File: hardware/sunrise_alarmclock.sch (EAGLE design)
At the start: 26 parts, among them IC1 ATMEGA328P, IC2 WTV020, IC3 TinyRTC, IC4 HC-05, IC5 LD117AS33TR

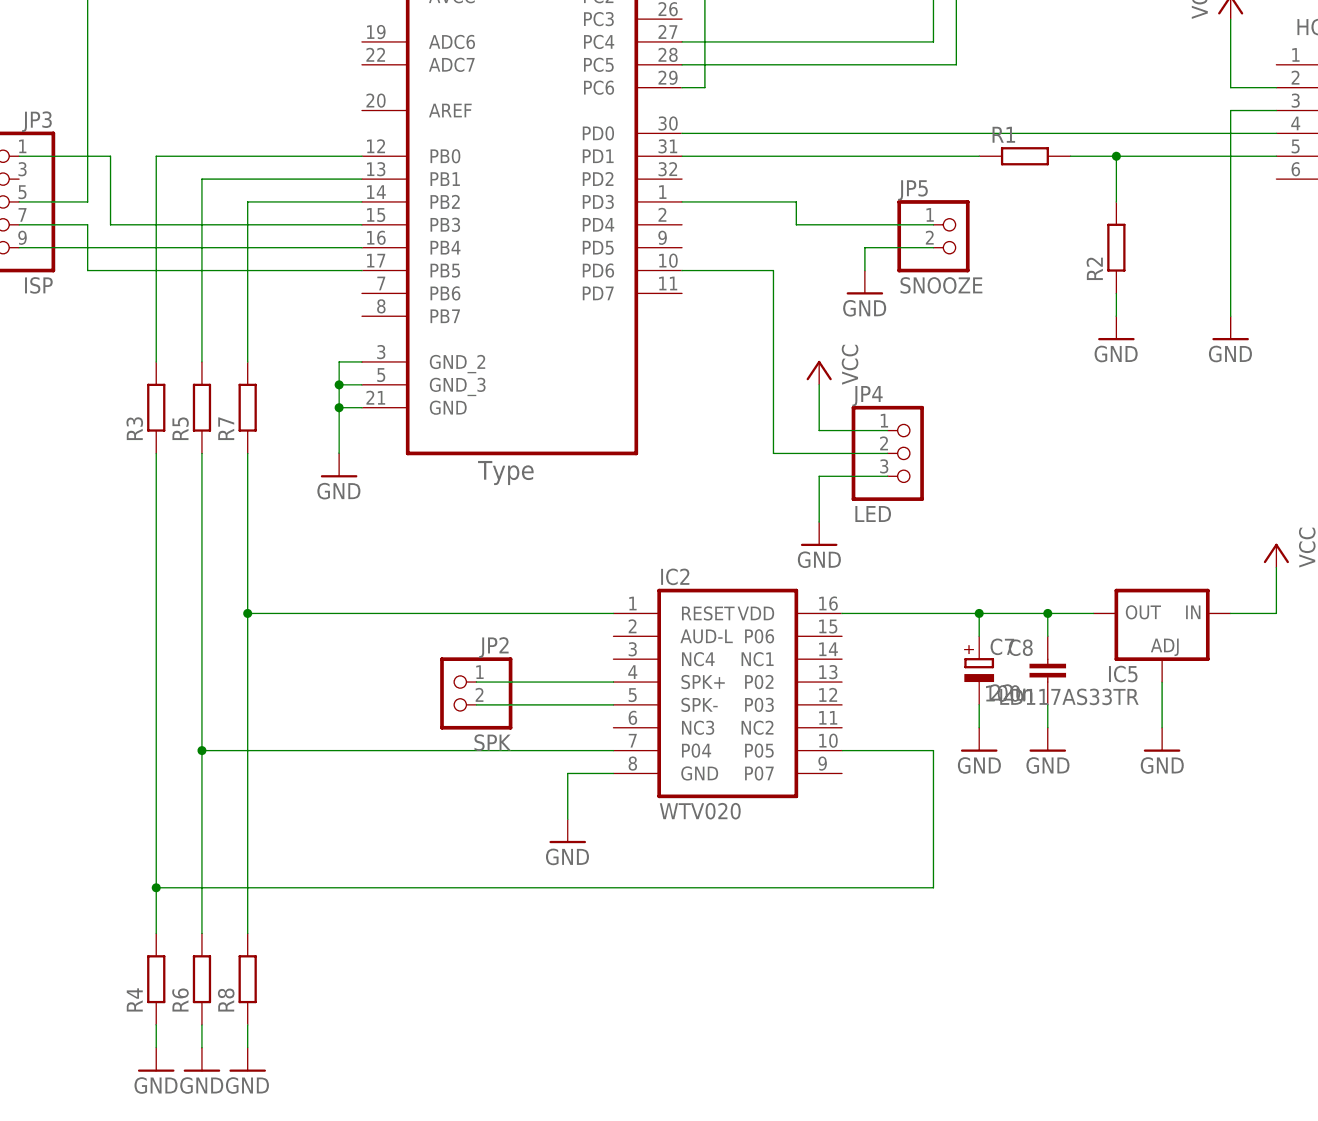
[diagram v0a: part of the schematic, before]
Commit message: hardware: added components values
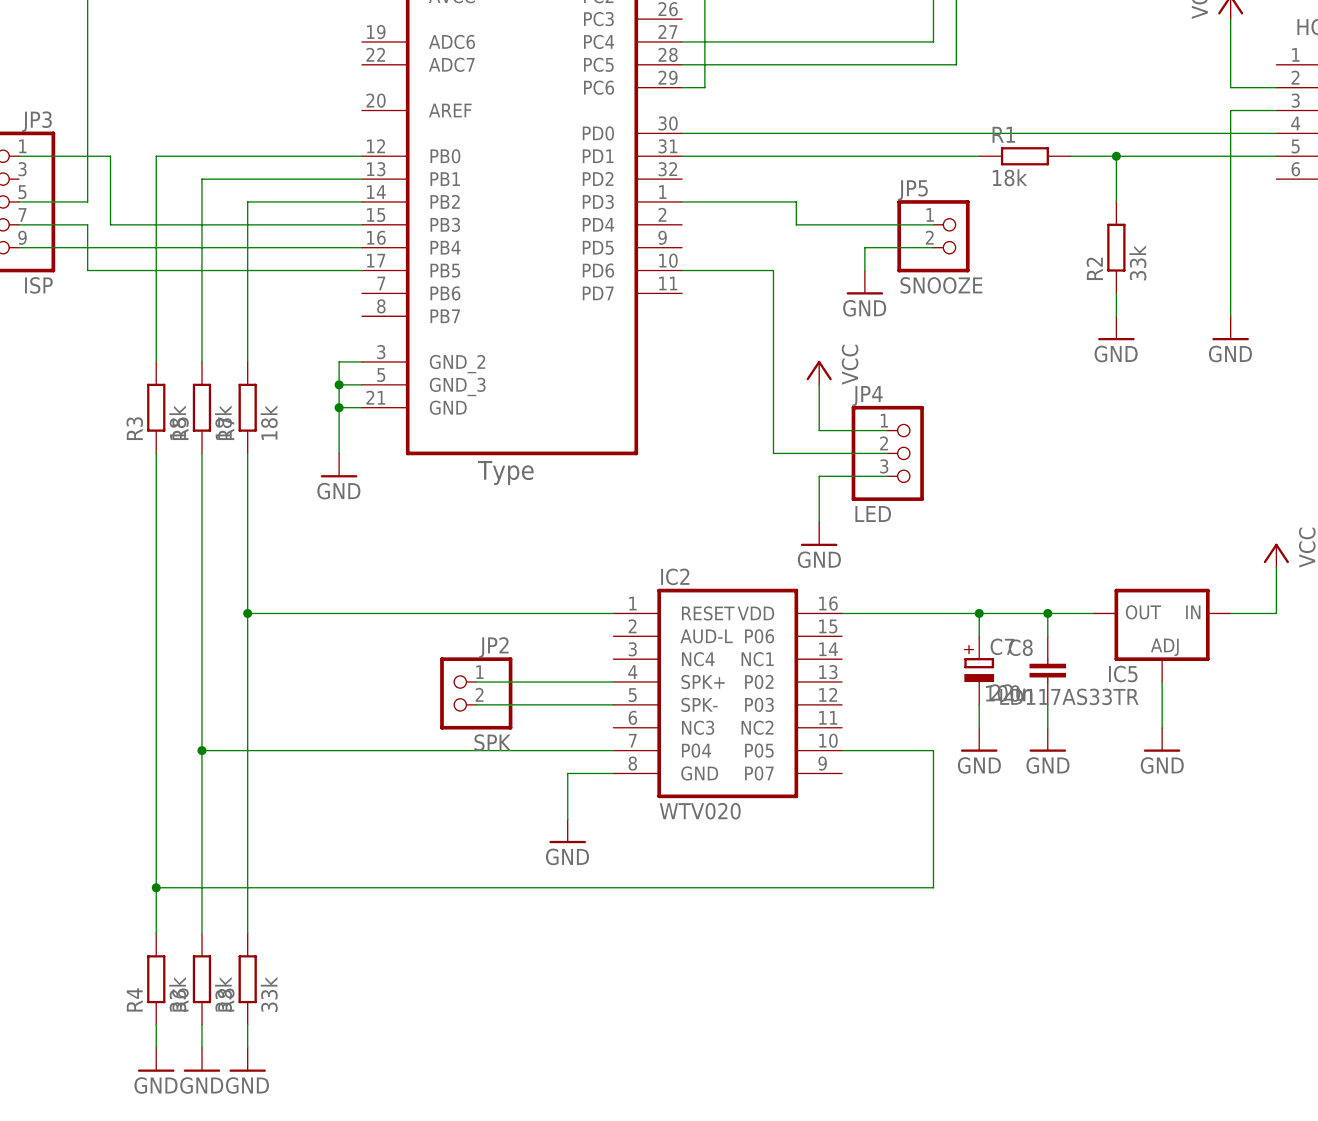
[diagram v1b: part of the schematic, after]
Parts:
- R1, R3, R5, R7: value (none) -> 18k
- R2, R4, R6, R8: value (none) -> 33k
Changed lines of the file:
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@@
 <part name="P+3" library="supply1" deviceset="VCC" device=""/>
 <part name="IC3" library="TinyRTC_module" deviceset="HC-05" device="" value="TinyRTC"/>
-<part name="R1" library="rcl" deviceset="R-EU_" device="M1206"/>
-<part name="R2" library="rcl" deviceset="R-EU_" device="M1206"/>
+<part name="R1" library="rcl" deviceset="R-EU_" device="M1206" value="18k"/>
+<part name="R2" library="rcl" deviceset="R-EU_" device="M1206" value="33k"/>
 <part name="C2" library="rcl" deviceset="C-EU" device="C1206K" value="100n"/>
 <part name="C3" library="rcl" deviceset="C-EU" device="C1206K" value="100n"/>
@@
 <part name="C8" library="rcl" deviceset="C-EU" device="C1206K" value="100n"/>
 <part name="GND7" library="supply1" deviceset="GND" device=""/>
-<part name="R3" library="rcl" deviceset="R-EU_" device="M1206"/>
-<part name="R5" library="rcl" deviceset="R-EU_" device="M1206"/>
-<part name="R7" library="rcl" deviceset="R-EU_" device="M1206"/>
-<part name="R4" library="rcl" deviceset="R-EU_" device="M1206"/>
-<part name="R6" library="rcl" deviceset="R-EU_" device="M1206"/>
-<part name="R8" library="rcl" deviceset="R-EU_" device="M1206"/>
+<part name="R3" library="rcl" deviceset="R-EU_" device="M1206" value="18k"/>
+<part name="R5" library="rcl" deviceset="R-EU_" device="M1206" value="18k"/>
+<part name="R7" library="rcl" deviceset="R-EU_" device="M1206" value="18k"/>
+<part name="R4" library="rcl" deviceset="R-EU_" device="M1206" value="33k"/>
+<part name="R6" library="rcl" deviceset="R-EU_" device="M1206" value="33k"/>
+<part name="R8" library="rcl" deviceset="R-EU_" device="M1206" value="33k"/>
 <part name="GND10" library="supply1" deviceset="GND" device=""/>
 <part name="GND11" library="supply1" deviceset="GND" device=""/>

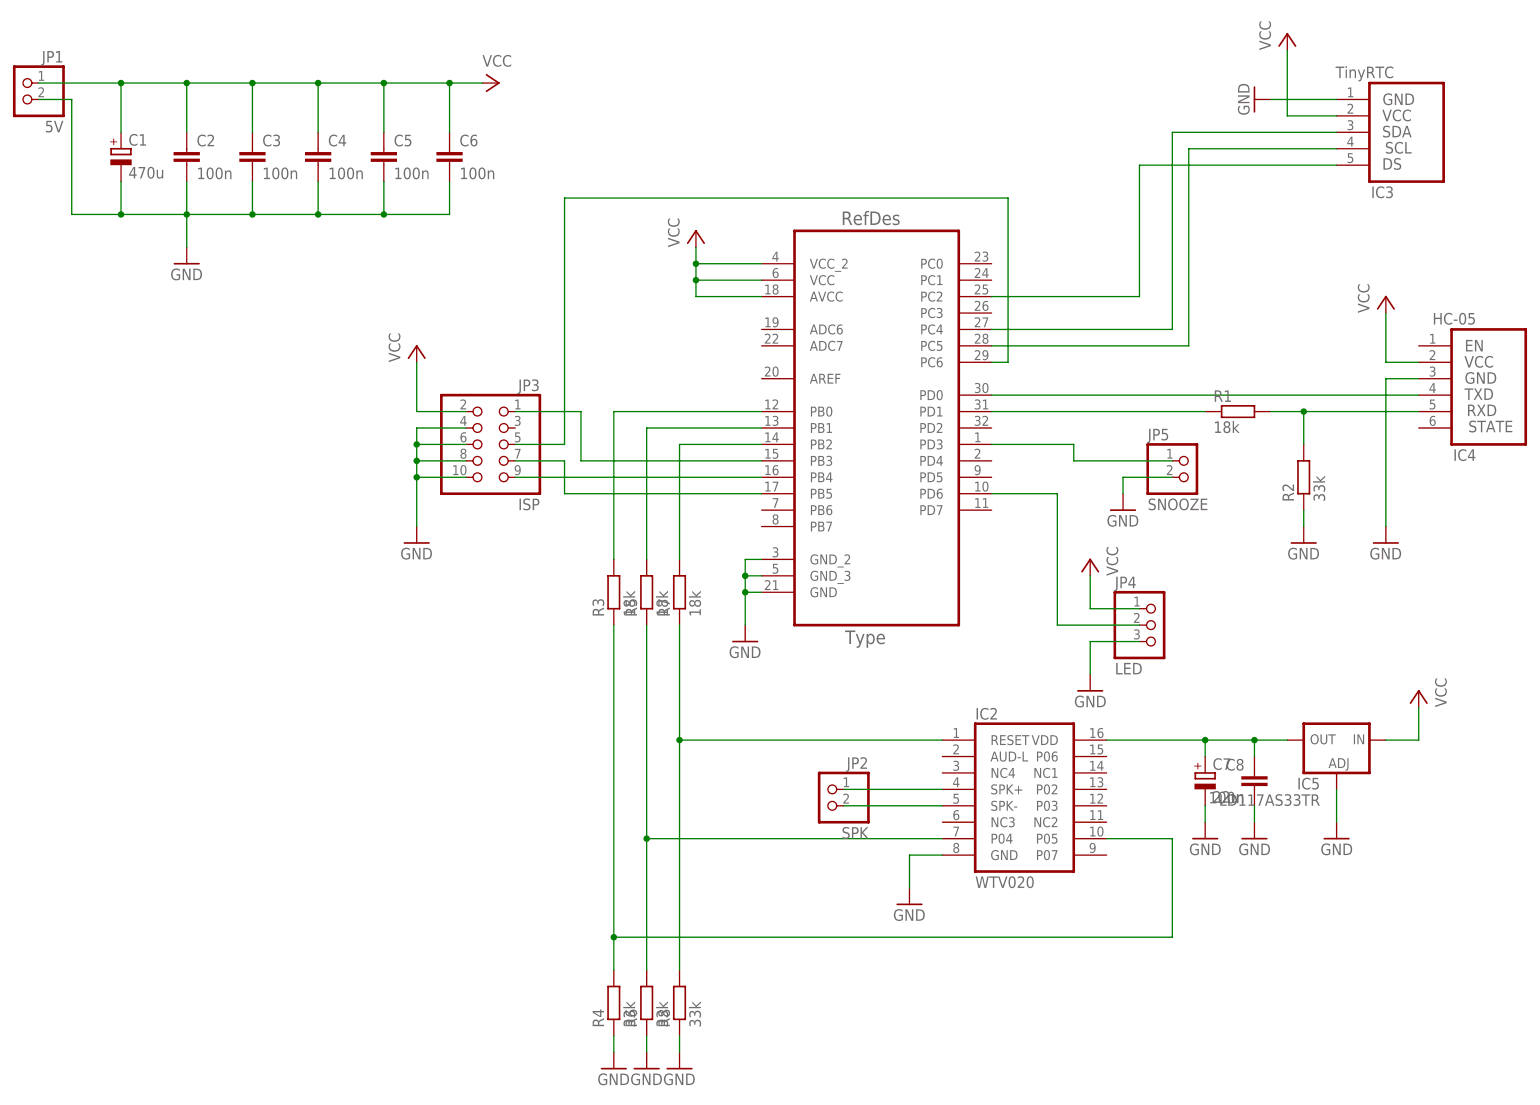
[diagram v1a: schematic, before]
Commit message: hardware: fixed values of resistor towards the voice module. added note about connection of photo resistor to pin PC1
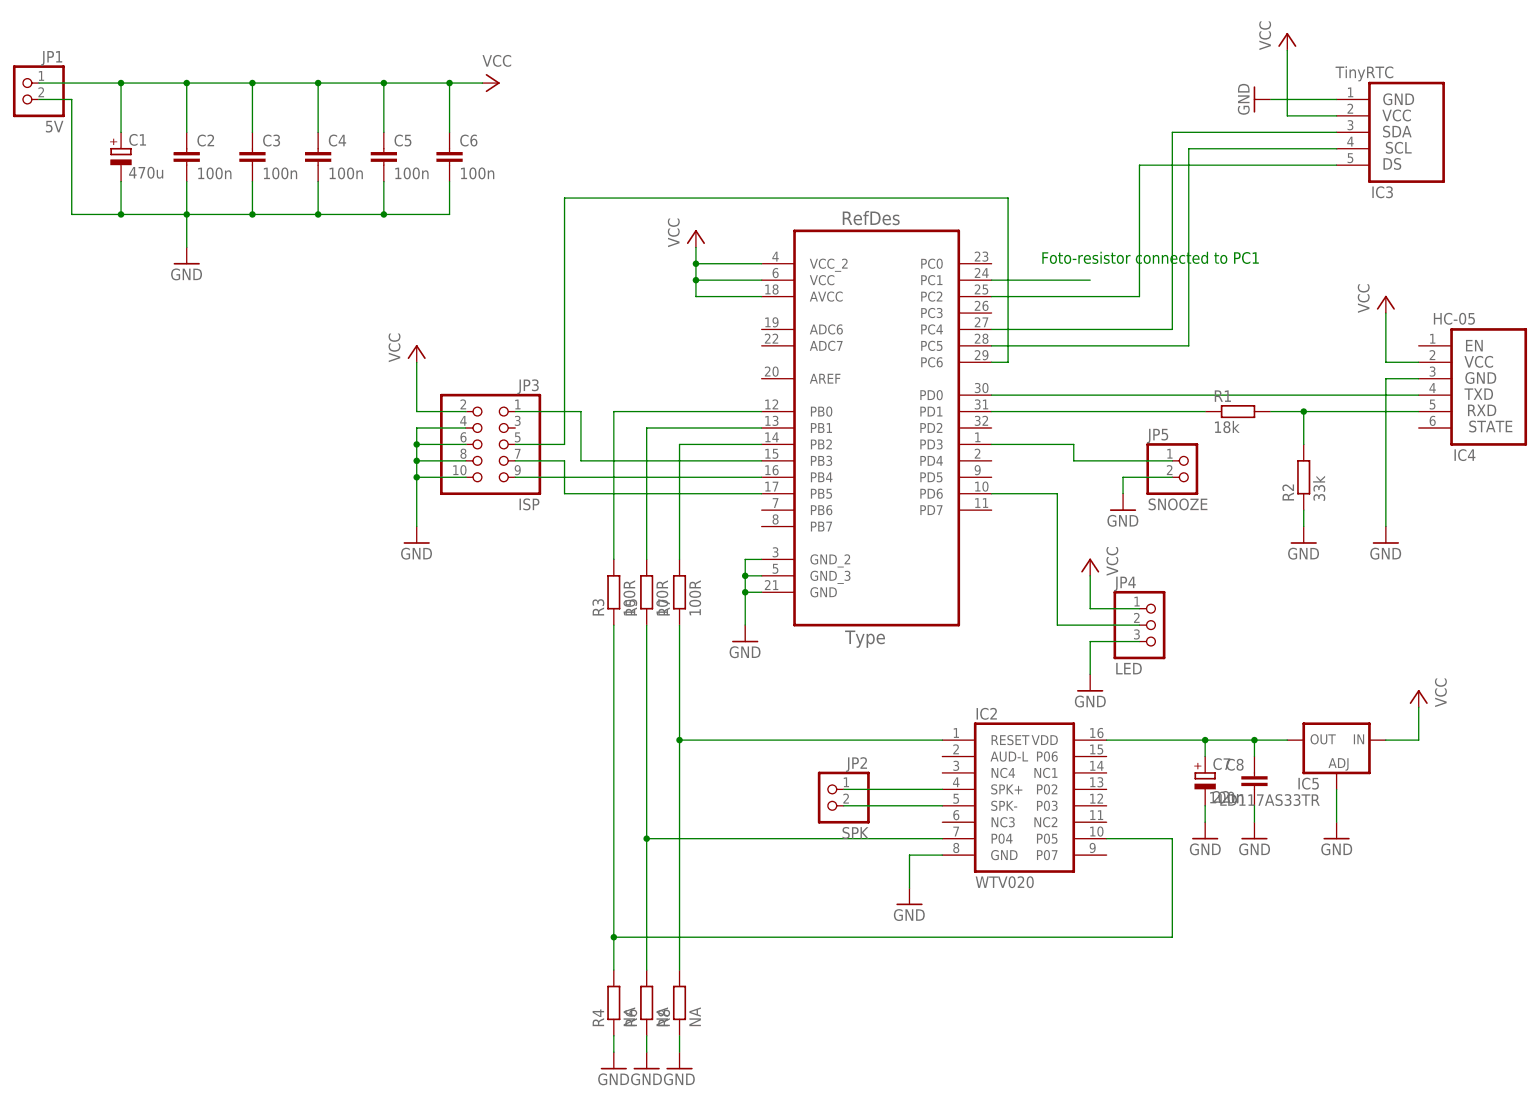
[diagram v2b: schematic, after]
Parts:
- R3, R5, R7: value 18k -> 100R
- R4, R6, R8: value 33k -> NA
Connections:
- new net N$22: IC1.PC1
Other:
- note added: "Foto-resistor connected to PC1"
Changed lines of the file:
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@@
 <part name="C8" library="rcl" deviceset="C-EU" device="C1206K" value="100n"/>
 <part name="GND7" library="supply1" deviceset="GND" device=""/>
-<part name="R3" library="rcl" deviceset="R-EU_" device="M1206" value="18k"/>
-<part name="R5" library="rcl" deviceset="R-EU_" device="M1206" value="18k"/>
-<part name="R7" library="rcl" deviceset="R-EU_" device="M1206" value="18k"/>
-<part name="R4" library="rcl" deviceset="R-EU_" device="M1206" value="33k"/>
-<part name="R6" library="rcl" deviceset="R-EU_" device="M1206" value="33k"/>
-<part name="R8" library="rcl" deviceset="R-EU_" device="M1206" value="33k"/>
+<part name="R3" library="rcl" deviceset="R-EU_" device="M1206" value="100R"/>
+<part name="R5" library="rcl" deviceset="R-EU_" device="M1206" value="100R"/>
+<part name="R7" library="rcl" deviceset="R-EU_" device="M1206" value="100R"/>
+<part name="R4" library="rcl" deviceset="R-EU_" device="M1206" value="NA"/>
+<part name="R6" library="rcl" deviceset="R-EU_" device="M1206" value="NA"/>
+<part name="R8" library="rcl" deviceset="R-EU_" device="M1206" value="NA"/>
 <part name="GND10" library="supply1" deviceset="GND" device=""/>
 <part name="GND11" library="supply1" deviceset="GND" device=""/>
@@
 <sheet>
 <plain>
+<text x="172.72" y="99.06" size="1.778" layer="91">Foto-resistor connected to PC1</text>
 </plain>
 <instances>
@@
 </segment>
 </net>
+<net name="N$22" class="0">
+<segment>
+<pinref part="IC1" gate="A" pin="PC1"/>
+<wire x1="165.1" y1="96.52" x2="180.34" y2="96.52" width="0.1524" layer="91"/>
+</segment>
+</net>
